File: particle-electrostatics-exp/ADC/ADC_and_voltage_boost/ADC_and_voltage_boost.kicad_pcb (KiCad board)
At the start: 2 copper layers, 117.2 x 46.8 mm, 24 parts, among them J1 Screw_Terminal_01x04, J2 Screw_Terminal_01x04, U4 MAX1032BEUG_

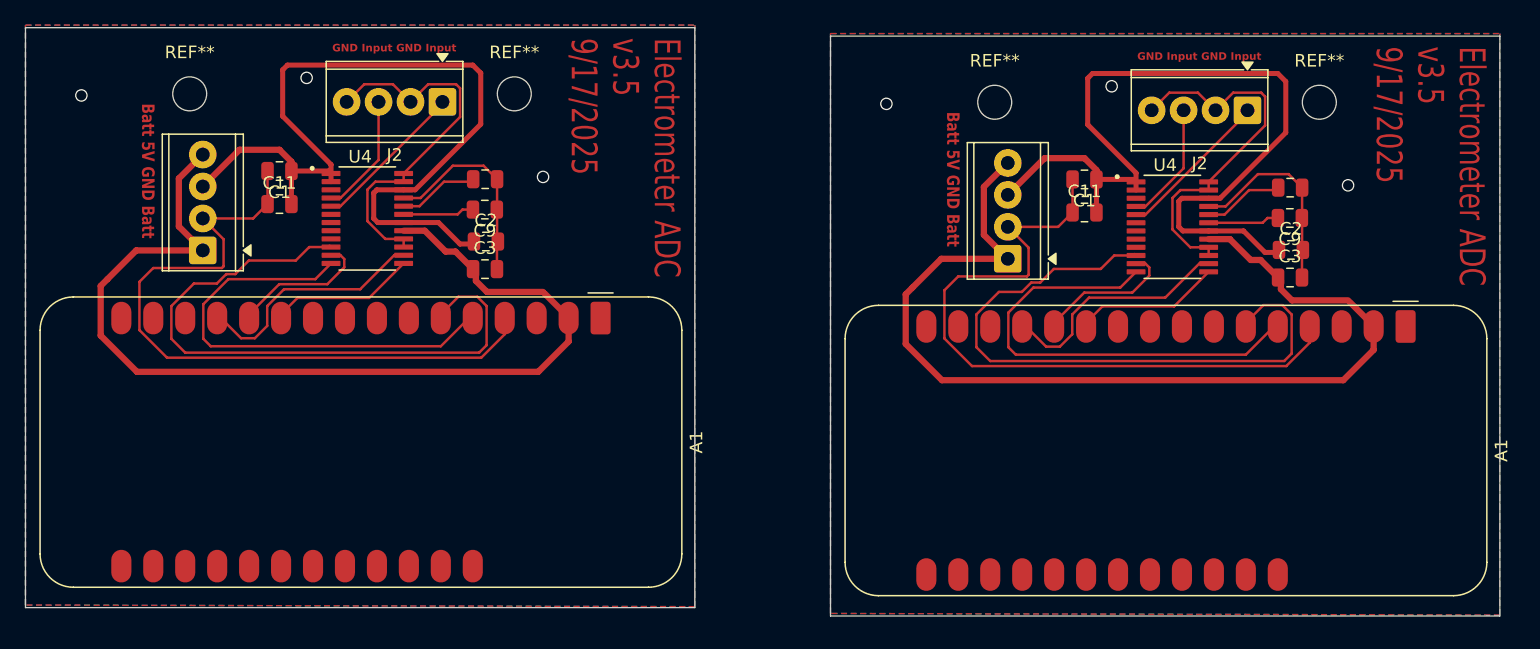
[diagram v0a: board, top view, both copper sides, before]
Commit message: updated pcb layout slightly
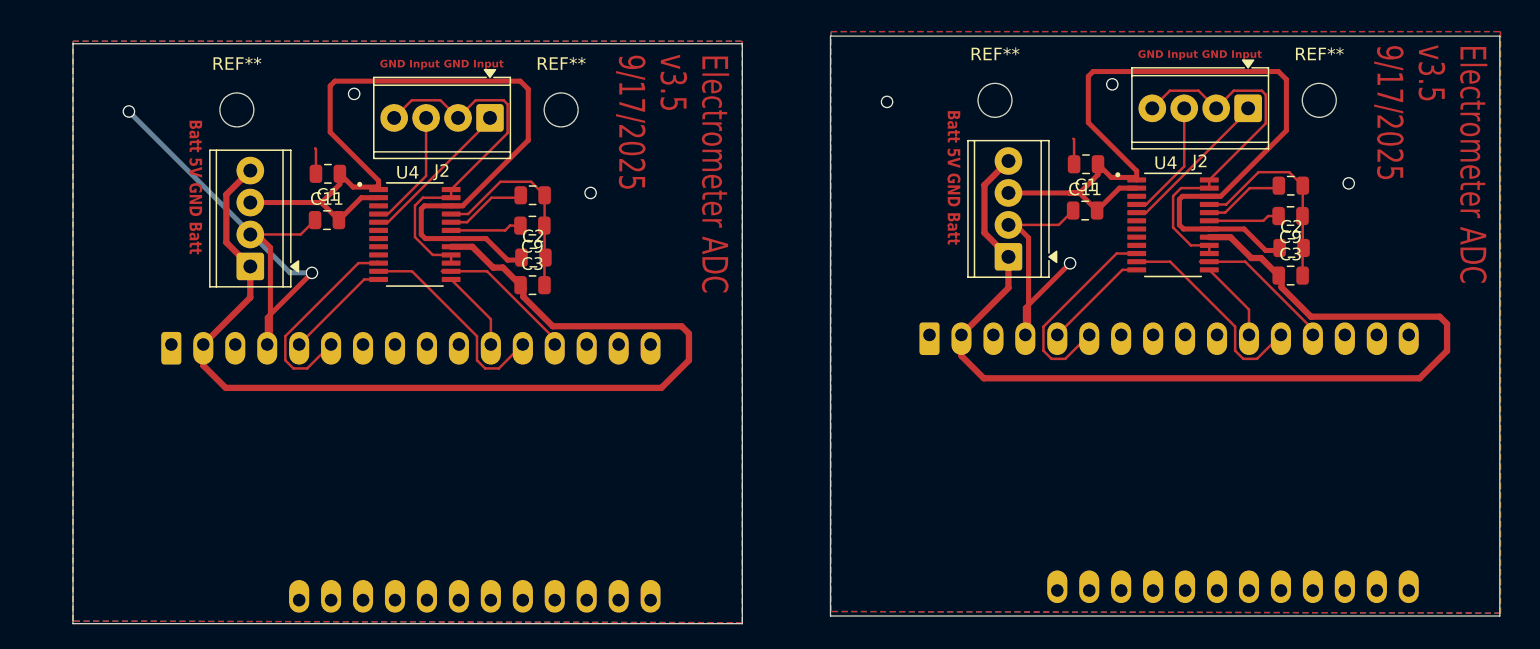
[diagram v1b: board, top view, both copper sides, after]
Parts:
- removed the A1 at (135.0, 98.5)
- removed the A1 at (199.0, 99.2)
- removed the C1 at (109.4, 87.2)
- removed the C1 at (173.4, 87.8)
- removed the C11 at (109.4, 89.8)
- removed the C11 at (173.4, 90.4)
- removed the C2 at (189.8, 93.4)
- removed the C2 at (125.8, 92.8)
- removed the C3 at (189.8, 95.6)
- removed the C3 at (125.8, 95.0)
- removed the C8 at (125.8, 87.8)
- removed the C8 at (189.8, 88.5)
- removed the C9 at (189.8, 90.9)
- removed the C9 at (125.8, 90.2)
- removed the J1 at (103.3, 93.5)
- removed the J1 at (167.3, 94.1)
- removed the J2 at (122.4, 81.7)
- removed the J2 at (186.4, 82.3)
- removed the REF** at (102.3, 81.0)
- removed the REF** at (166.3, 81.7)
- removed the REF** at (192.1, 81.7)
- removed the REF** at (128.1, 81.0)
- removed the U4 at (180.4, 91.6)
- removed the U4 at (116.4, 90.9)
- added A1: Adafruit_Feather_Generic, Module:Adafruit_Feather, B.Cu at (100.8, 100.9)
- added A1: Adafruit_Feather_Generic, Module:Adafruit_Feather, B.Cu at (161.1, 100.2)
- added C1: 100n, Capacitor_SMD:C_0805_2012Metric, F.Cu at (173.6, 86.6)
- added C1: 100n, Capacitor_SMD:C_0805_2012Metric, F.Cu at (113.3, 87.4)
- added C11: 100n, Capacitor_SMD:C_0805_2012Metric, F.Cu at (173.5, 90.3)
- added C11: 100n, Capacitor_SMD:C_0805_2012Metric, F.Cu at (113.2, 91.1)
- added C2: 100n, Capacitor_SMD:C_0805_2012Metric, F.Cu at (189.9, 93.3)
- added C2: 100n, Capacitor_SMD:C_0805_2012Metric, F.Cu at (129.6, 94.0)
- added C3: 100n, Capacitor_SMD:C_0805_2012Metric, F.Cu at (189.8, 95.5)
- added C3: 100n, Capacitor_SMD:C_0805_2012Metric, F.Cu at (129.6, 96.2)
- added C8: 1u, Capacitor_SMD:C_0805_2012Metric, F.Cu at (129.6, 89.1)
- added C8: 1u, Capacitor_SMD:C_0805_2012Metric, F.Cu at (189.8, 88.3)
- added C9: 100n, Capacitor_SMD:C_0805_2012Metric, F.Cu at (189.8, 90.7)
- added C9: 100n, Capacitor_SMD:C_0805_2012Metric, F.Cu at (129.5, 91.5)
- added J1: Screw_Terminal_01x04, TerminalBlock_Phoenix:TerminalBlock_Phoenix_MPT-0,5-4-2.54_1x04_P2.54mm_Horizontal, F.Cu at (167.4, 94.0)
- added J1: Screw_Terminal_01x04, TerminalBlock_Phoenix:TerminalBlock_Phoenix_MPT-0,5-4-2.54_1x04_P2.54mm_Horizontal, F.Cu at (107.1, 94.7)
- added J2: Screw_Terminal_01x04, TerminalBlock_Phoenix:TerminalBlock_Phoenix_MPT-0,5-4-2.54_1x04_P2.54mm_Horizontal, F.Cu at (126.2, 82.9)
- added J2: Screw_Terminal_01x04, TerminalBlock_Phoenix:TerminalBlock_Phoenix_MPT-0,5-4-2.54_1x04_P2.54mm_Horizontal, F.Cu at (186.4, 82.2)
- added REF**: MountingHole_2.7mm, MountingHole:MountingHole_2.7mm, F.Cu at (166.3, 81.5)
- added REF**: MountingHole_2.7mm, MountingHole:MountingHole_2.7mm, F.Cu at (131.8, 82.3)
- added REF**: MountingHole_2.7mm, MountingHole:MountingHole_2.7mm, F.Cu at (106.0, 82.3)
- added REF**: MountingHole_2.7mm, MountingHole:MountingHole_2.7mm, F.Cu at (192.1, 81.5)
- added U4: MAX1032BEUG_, Max1032:SOP65P640X110-24N, F.Cu at (120.2, 92.2)
- added U4: MAX1032BEUG_, Max1032:SOP65P640X110-24N, F.Cu at (180.5, 91.4)
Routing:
- net /~{CS}: track 101.6 -> 33.2 mm
- net /SSTRB: track 73.9 -> 16.9 mm
- net GND: track 204.6 -> 161.7 mm, vias 6 -> 8
- net /MISO: track 38.5 -> 23.3 mm
- net /MOSI: track 21.9 -> 33.1 mm
- net /SCK: track 22.8 -> 13.0 mm
- net +BATT: track 160.2 -> 166.4 mm
- net +5V: track 135.3 -> 141.2 mm
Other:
- board size 117.2 x 46.8 mm -> 113.4 x 46.7 mm

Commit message: slight changes to adc board
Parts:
- removed the REF** at (166.3, 81.5)
- removed the REF** at (192.1, 81.5)
- added REF**: MountingHole_2.7mm, MountingHole:MountingHole_2.7mm, F.Cu at (192.0, 81.9)
- added REF**: MountingHole_2.7mm, MountingHole:MountingHole_2.7mm, F.Cu at (166.3, 81.9)
- moved C1 1.02 mm to (114.2, 86.9), turned to 90 degrees
- moved C11 0.98 mm to (114.2, 90.9), turned to 90 degrees
- moved C11 0.92 mm to (174.4, 90.5), turned to 90 degrees
- moved C1 0.85 mm to (174.4, 86.5), turned to 90 degrees
- moved A1 0.35 mm to (161.1, 100.5)
- moved C8 0.35 mm to (189.8, 88.7)
- moved C9 0.35 mm to (189.8, 91.1)
- moved J1 0.35 mm to (167.3, 94.3)
- moved J2 0.35 mm to (186.4, 82.5)
- moved U4 0.35 mm to (180.4, 91.8)
- moved C2 0.35 mm to (189.8, 93.6)
- moved C3 0.35 mm to (189.8, 95.8)
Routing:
- net GND: track 161.7 -> 141.8 mm
- net +BATT: track 166.4 -> 173.4 mm
- net +5V: track 141.2 -> 136.8 mm
